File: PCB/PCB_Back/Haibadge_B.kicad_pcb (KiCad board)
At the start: 2 copper layers, 80 x 80 mm, 69 parts, among them J1 Sensor connector, J2 USB_C_Receptacle_USB2.0, J3 Lipo connector, Q1 UMH3N, Q2 PMOS, SW1 SW_Push_Dual, U1 ESP-12E, U2 CH340C, U3 MCP73831-2-OT, U4 MCP1700x-330xxTT, U6 BME680

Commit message: Layout, Routing, Stuff
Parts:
- removed H4, H5: MountingHole, MountingHole:MountingHole_2.7mm_M2.5
- added ? (x5): , Graphics, F.Cu at (100.0, 100.0)
- added ? (x3): , Graphics, F.Cu at (200.0, 47.5)
- added C24: 100nF, Capacitor_SMD:C_0805_2012Metric, B.Cu at (134.0, 164.6)
- added C25: 100nF, Capacitor_SMD:C_0805_2012Metric, B.Cu at (147.0, 161.0)
- C16, C19, C20, C21, C22, C23, D16, D17, J1, J2, J3, Q1, Q2, R10, R11, R12, R13, R2, R4, R5, R6, R7, R8, SW1, U1, U2, U3, U4: moved to B.Cu
- R9: footprint Resistor_SMD:R_0815_2038Metric -> Resistor_SMD:R_0805_2012Metric; moved to B.Cu
- U6: footprint KH-6X6X6H-STM:KH-6X6X6H-STM -> Package_LGA:Bosch_LGA-8_3x3mm_P0.8mm_ClockwisePinNumbering
- moved D7 120.8 mm to (140.6, 170.8)
- moved H3 118.1 mm to (150.3, 153.8)
- moved C7 117.3 mm to (139.0, 166.0)
- moved R5 112.4 mm to (143.0, 169.4), turned to 90 degrees
- moved H2 111.8 mm to (130.0, 153.8)
- moved C8 111.1 mm to (121.0, 160.0)
- moved J2 109.4 mm to (140.2, 176.9), turned to 180 degrees
- moved R6 107.8 mm to (137.0, 169.4), turned to -90 degrees
- moved D8 107.6 mm to (122.5, 164.8)
- moved R7 105.6 mm to (139.1, 169.4), turned to 90 degrees
- moved R8 103.4 mm to (141.0, 169.4), turned to -90 degrees
- moved U2 102.8 mm to (140.6, 163.0), turned to 90 degrees
- moved C17 101.2 mm to (139.9, 143.8), turned to -90 degrees
- moved C9 100.9 mm to (117.5, 151.5)
- moved C18 99.4 mm to (142.0, 143.8), turned to -90 degrees
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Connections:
- D11 pad 4: Net-(D11-DIN) -> Net-(D10-DOUT)
- D12 pad 4: Net-(D12-DIN) -> Net-(D11-DOUT)
- D13 pad 4: Net-(D10-DOUT) -> Net-(D12-DOUT)
- D14 pad 4: Net-(D11-DOUT) -> Net-(D13-DOUT)
- D15 pad 4: Net-(D12-DOUT) -> Net-(D14-DOUT)
- D2 pad 4: Net-(D13-DOUT) -> Net-(D1-DOUT)
- D3 pad 4: Net-(D14-DOUT) -> Net-(D2-DOUT)
- D4 pad 4: Net-(D1-DOUT) -> Net-(D3-DOUT)
- D5 pad 4: Net-(D2-DOUT) -> Net-(D4-DOUT)
- D6 pad 4: Net-(D3-DOUT) -> Net-(D5-DOUT)
- D7 pad 2: Net-(D10-DIN) -> Net-(D7-DOUT)
- D7 pad 4: Net-(D4-DOUT) -> Net-(D6-DOUT)
- D8 pad 2: Net-(D11-DIN) -> Net-(D8-DOUT)
- D8 pad 4: Net-(D5-DOUT) -> Net-(D7-DOUT)
- D9 pad 2: Net-(D12-DIN) -> Net-(D10-DIN)
- D9 pad 4: Net-(D6-DOUT) -> Net-(D8-DOUT)
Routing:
- net VCC: track 0.00 -> 288.0 mm, vias 0 -> 1
- net +3V3: track 0.00 -> 188.4 mm, vias 0 -> 5
- net RST: track 0.00 -> 92.6 mm, vias 0 -> 2
- net +5V: track 0.00 -> 87.4 mm, vias 0 -> 1
- net Sensor: track 0.00 -> 58.9 mm, vias 0 -> 5
- net Net-(U1-GPIO3/RXD): track 0.00 -> 51.9 mm, vias 0 -> 4
- net Net-(U1-GPIO1/TXD): track 0.00 -> 51.7 mm, vias 0 -> 2
- net GPIO0: track 0.00 -> 41.0 mm, vias 0 -> 2
- net +BATT: track 0.00 -> 33.6 mm
- net Net-(U1-GPIO5): track 0.00 -> 24.6 mm, vias 0 -> 1
- net Net-(U1-GPIO4): track 0.00 -> 22.3 mm, vias 0 -> 1
- net Net-(D3-DOUT): track 0.00 -> 20.3 mm
- net Net-(D8-DOUT): track 0.00 -> 20.1 mm
- net Net-(D10-DIN): track 0.00 -> 18.4 mm
- net Net-(D4-DOUT): track 0.00 -> 17.9 mm
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- added copper zone on B.Cu, net GND
- added copper zone on F.Cu, net GND
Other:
- board size 80 x 80 mm -> 79.8 x 79.8 mm
- board text added: "${REFERENCE}"

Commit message: Label placements, Misc Fixes, Partslist
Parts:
- moved Q2 0.36 mm to (105.2, 141.8)
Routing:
- net +5V: track 87.4 -> 71.7 mm, vias 1 -> 3
- net +3V3: track 188.4 -> 200.9 mm, vias 5 -> 6
- net GND: track 0.00 -> 5.95 mm, vias 114 -> 138
- net /uC/D+: track 2.84 -> 5.96 mm
- net /uC/D-: track 2.97 -> 5.96 mm, vias 0 -> 2
- net Net-(U1-GPIO4): track 22.3 -> 23.1 mm
- net Net-(U1-GPIO5): track 24.6 -> 25.4 mm
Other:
- board text added: "Blahaj Pentgramm Badge v1.0 (2024) Waldo und nicht Peter"
- board text added: "D9"
- board text added: "v.1.0"
- board text removed: "${REFERENCE}"

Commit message: Misc. Fixes, v1.0.
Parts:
- removed Q2: PMOS, Package_TO_SOT_SMD:SOT-23
- added Q3: Q_PMOS_GSD, Package_TO_SOT_SMD:SOT-23, B.Cu at (104.7, 141.9)
- added SW2: SW_PWR, easyeda2kicad:SW-SMD_MK-12C02-G025, B.Cu at (115.8, 168.1)
- D16: footprint LED_SMD:LED_0805_2012Metric -> LED_SMD:LED_1206_3216Metric
- moved R4 1.64 mm to (108.9, 154.1)
- moved D16 0.45 mm to (113.5, 154.0)
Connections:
- C20 pad 1: VCC -> Net-(D17-K)
- D17 pad 1: VCC -> Net-(D17-K)
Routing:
- net Net-(D17-K): track 0.00 -> 32.8 mm, vias 0 -> 2
- net +5V: track 71.7 -> 74.7 mm
- net +BATT: track 33.9 -> 35.5 mm
- net Net-(D16-A): track 1.65 -> 2.40 mm
- net VCC: track 288.1 -> 287.6 mm, vias 1 -> 2
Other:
- board text added: "+"
- board text added: "-"
- board text added: "RESET"
- board text added: "off"
- board text added: "on"

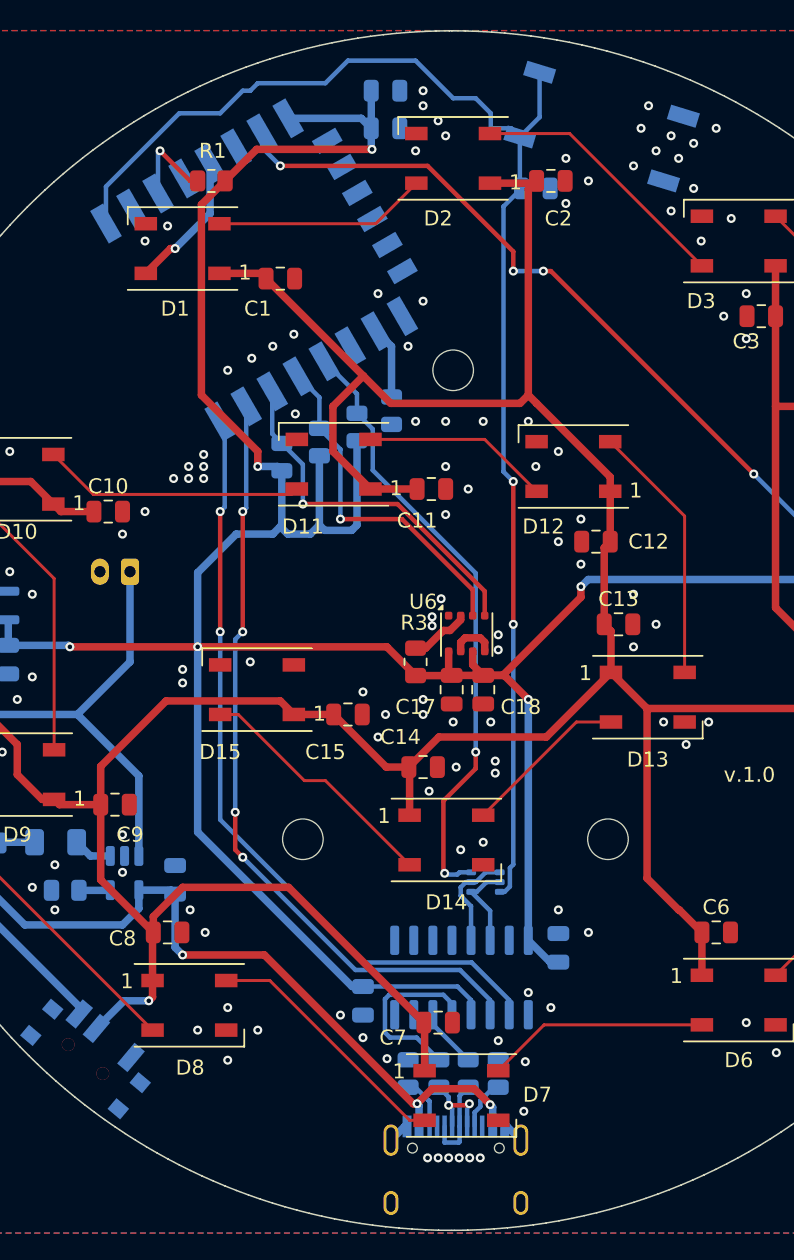
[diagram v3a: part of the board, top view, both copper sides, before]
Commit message: Switched D+/D-, TX/RX, Switch Pins and rotated Lipo Marking
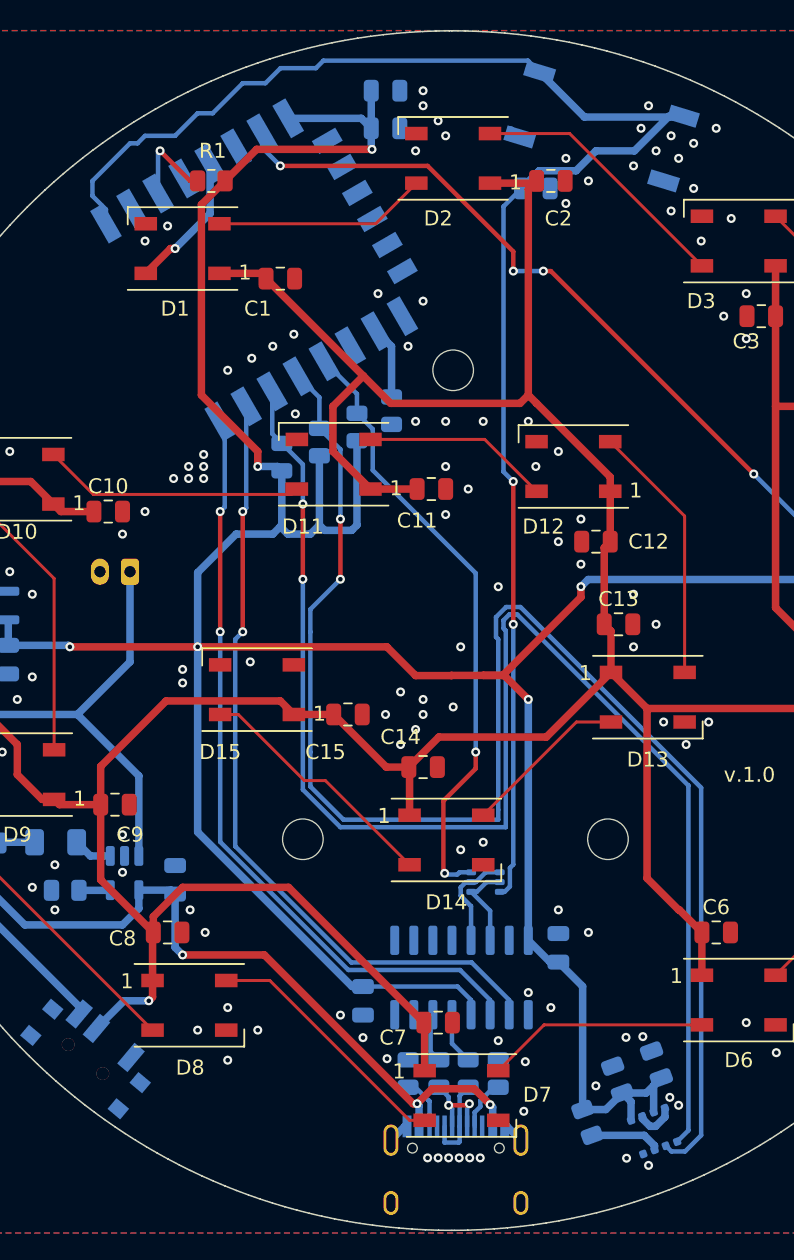
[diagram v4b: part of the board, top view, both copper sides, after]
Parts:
- C17, C18, R3, U6: moved to B.Cu
- moved U6 35.4 mm to (153.4, 173.2), turned to 20 degrees
- moved R3 32.7 mm to (148.9, 172.6), turned to 110 degrees
- moved C17 28.2 mm to (150.9, 169.8), turned to 110 degrees
- moved C18 27.5 mm to (153.5, 168.8), turned to 110 degrees
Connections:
- SW1 pad 1: GND -> RST
- SW1 pad 4: RST -> GND
- U2 pad 2: Net-(U1-GPIO1/TXD) -> Net-(U1-GPIO3/RXD)
- U2 pad 3: Net-(U1-GPIO3/RXD) -> Net-(U1-GPIO1/TXD)
- U2 pad 5: /uC/RD- -> /uC/RD+
- U2 pad 6: /uC/RD+ -> /uC/RD-
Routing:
- net Net-(U1-GPIO4): track 23.1 -> 101.2 mm, vias 1 -> 2
- net Net-(U1-GPIO5): track 25.4 -> 97.8 mm, vias 1 -> 2
- net +3V3: track 200.9 -> 218.9 mm
- net RST: track 92.6 -> 108.5 mm
- net /uC/RD-: track 12.1 -> 3.29 mm
- net Net-(U1-GPIO3/RXD): track 51.9 -> 53.0 mm, vias 4 -> 2
- net Net-(U6-CSB): track 4.06 -> 4.72 mm
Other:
- board text added: "Blahaj Pentgramm Badge v2.0 (2024) Waldo und vielleicht Peter"
- board text removed: "Blahaj Pentgramm Badge v1.0 (2024) Waldo und nicht Peter"

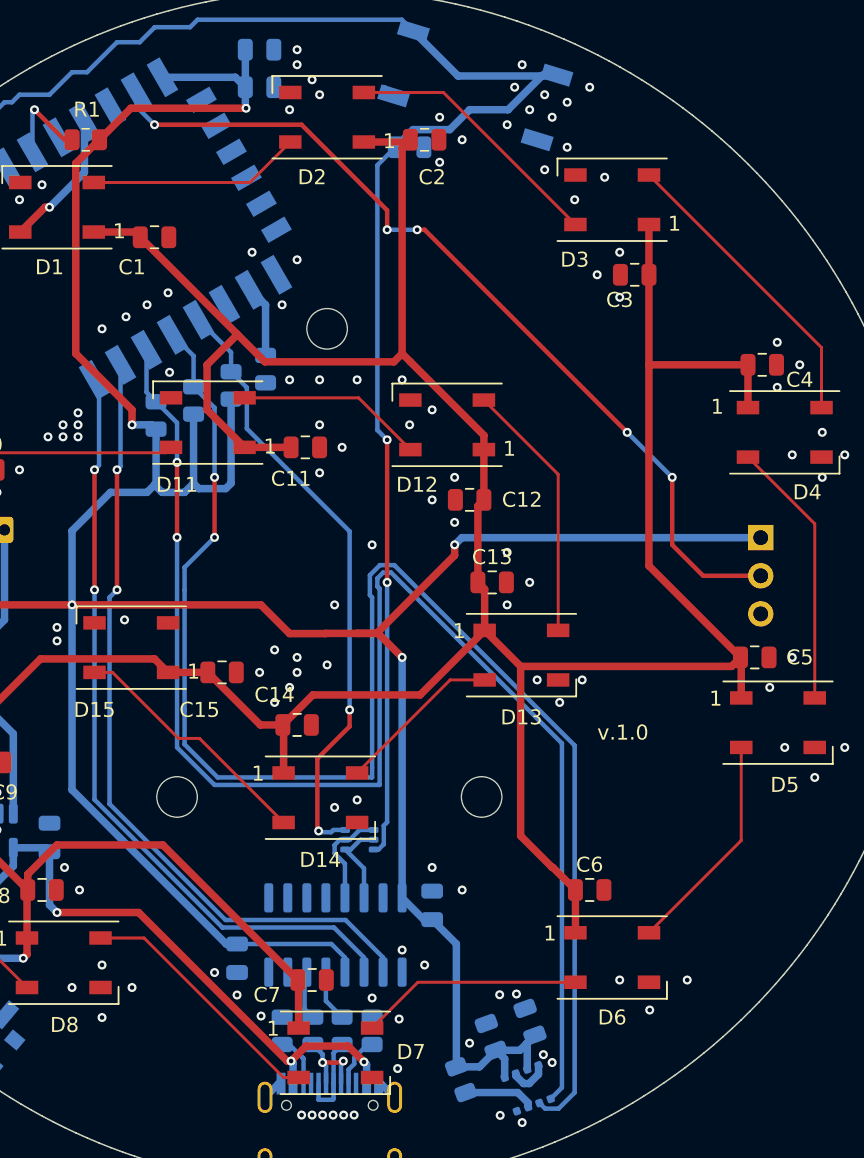
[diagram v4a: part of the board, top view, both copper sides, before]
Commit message: Moved Sensor Connector (make Room for Lipo) and Align with Pentagram Angle
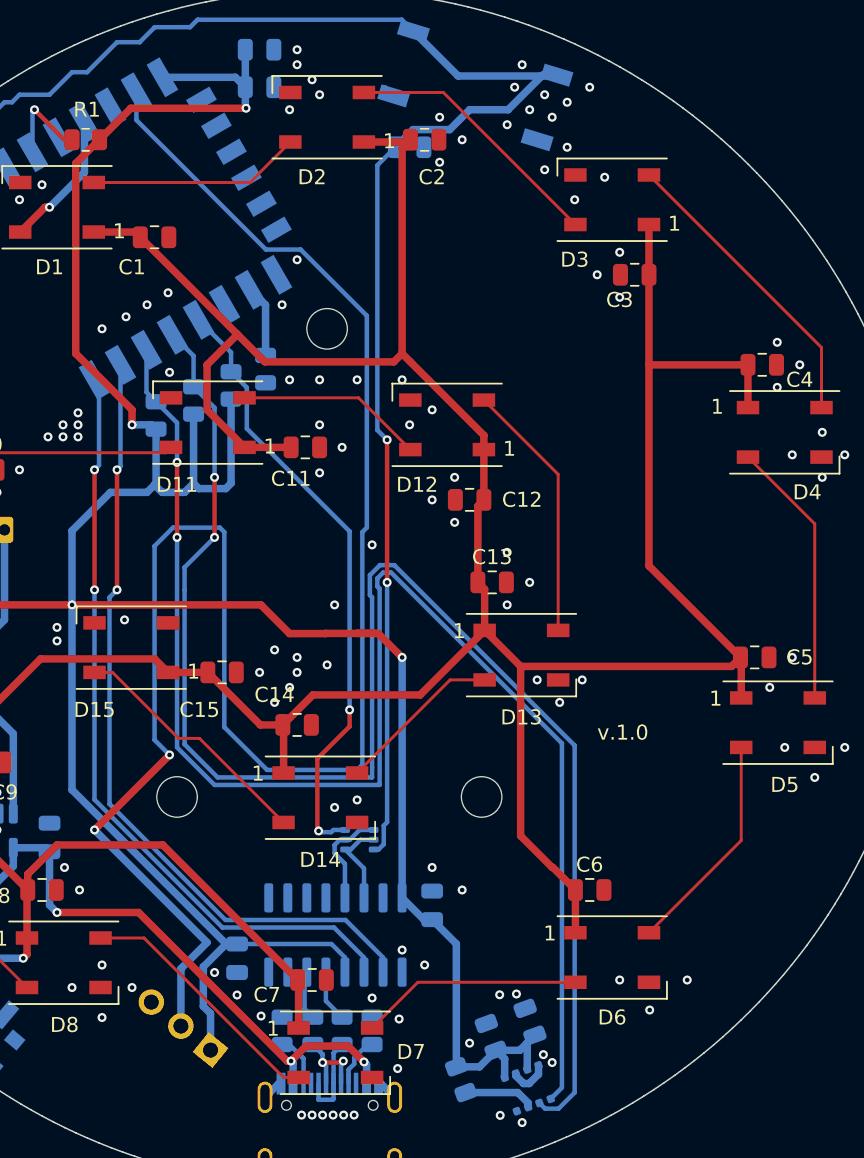
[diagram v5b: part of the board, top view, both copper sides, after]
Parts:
- moved J1 50.1 mm to (132.2, 170.7), turned to 51 degrees
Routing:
- net Sensor: track 58.9 -> 119.9 mm, vias 5 -> 2
- net +3V3: track 218.9 -> 198.2 mm, vias 6 -> 5
- net GND: vias 138 -> 137

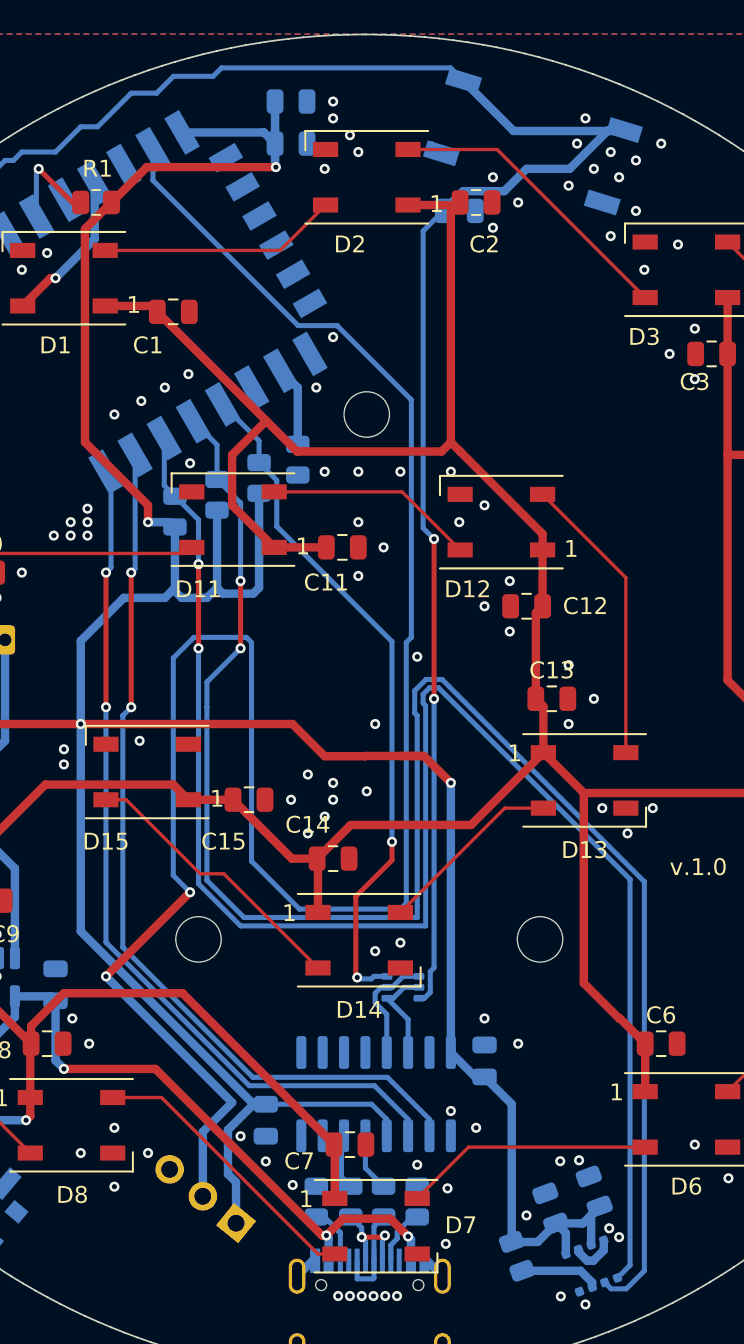
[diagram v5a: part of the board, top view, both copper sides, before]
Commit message: Moved Sensor again (inset), Work on Case
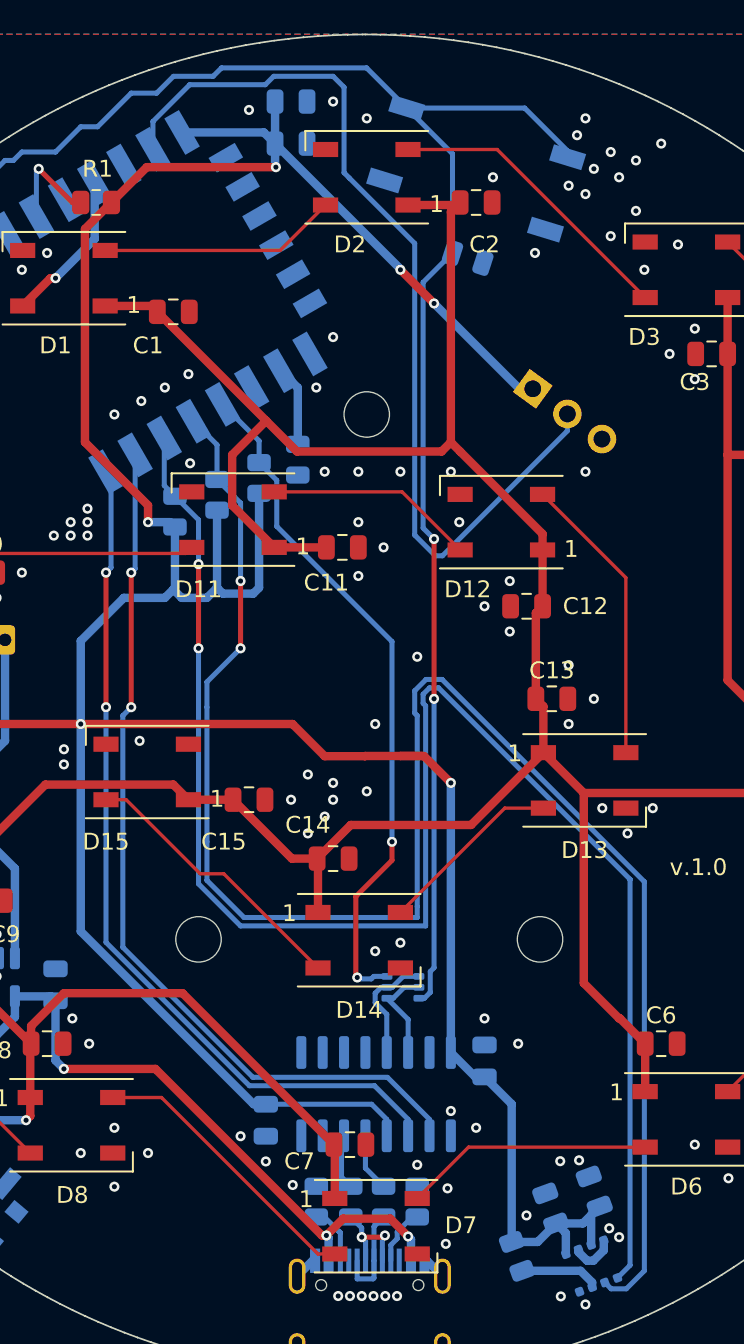
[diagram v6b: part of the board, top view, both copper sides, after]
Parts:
- removed the ? at (200.0, 47.5) (x3)
- added ?: , Graphics, F.Cu at (186.2, 101.2)
- moved J1 52.6 mm to (149.9, 121.1), turned to -126 degrees
- moved SW1 3.74 mm to (146.5, 108.0)
- moved C16 2.84 mm to (146.0, 113.3), turned to -18 degrees
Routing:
- net Sensor: track 119.9 -> 56.4 mm, vias 2 -> 0
- net +3V3: track 198.2 -> 211.6 mm, vias 5 -> 7
- net RST: track 108.5 -> 100.5 mm
- net GND: track 6.43 -> 5.61 mm, vias 137 -> 135
